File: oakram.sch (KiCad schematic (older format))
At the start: 4 parts, among them U1 DRAM_1MX16_SOJ, U2 DRAM_1MX16_SOJ, X1 ZIP40, X2 ZIP40

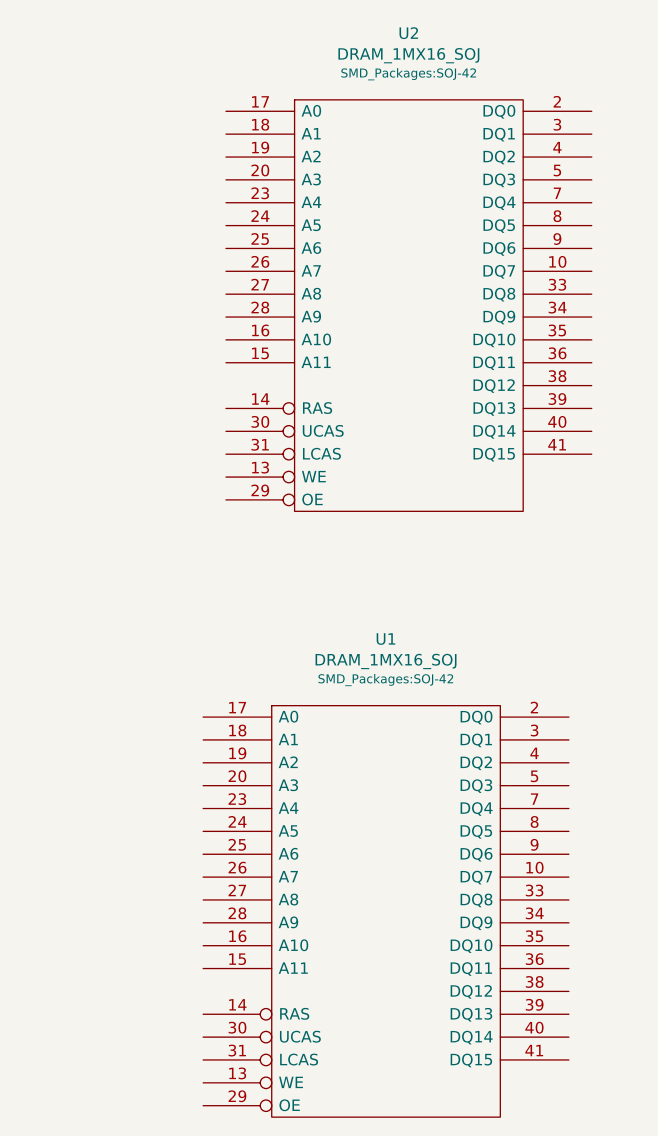
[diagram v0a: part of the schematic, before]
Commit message: Some bus signals assigned
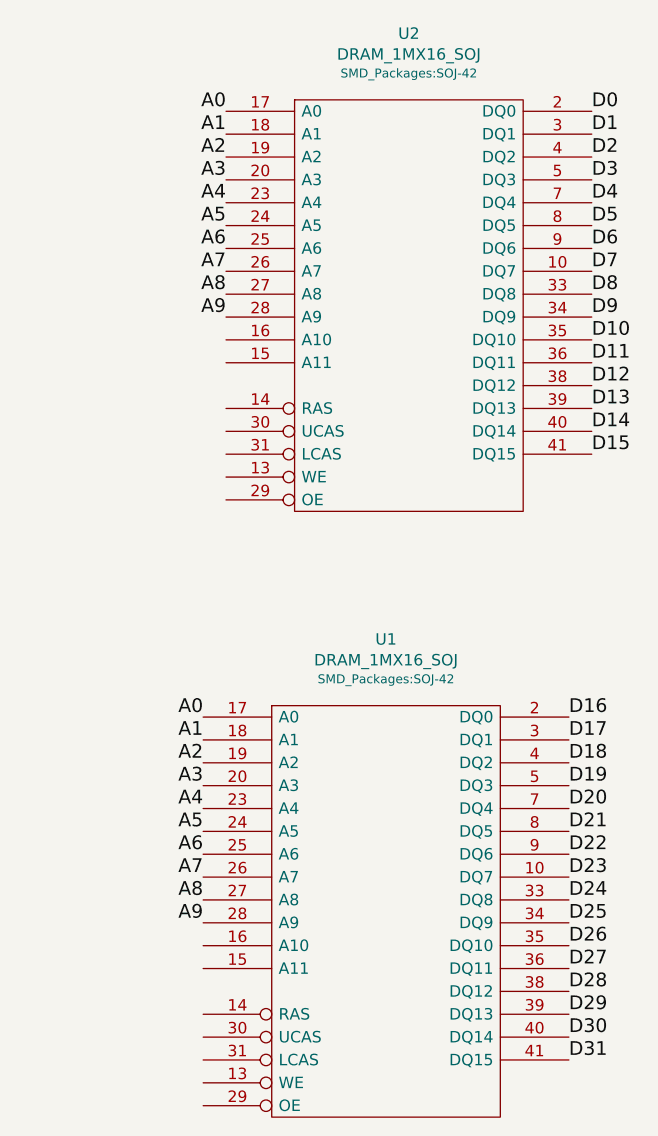
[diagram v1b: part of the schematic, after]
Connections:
- net A0: now also U1.17 (A0), U2.17 (A0)
- net A1: now also U1.18 (A1), U2.18 (A1)
- net A2: now also U1.19 (A2), U2.19 (A2)
- net A3: now also U1.20 (A3), U2.20 (A3)
- net A4: now also U1.23 (A4), U2.23 (A4)
- net A5: now also U1.24 (A5), U2.24 (A5)
- net A6: now also U1.25 (A6), U2.25 (A6)
- net A7: now also U1.26 (A7), U2.26 (A7)
- net A8: now also U1.27 (A8), U2.27 (A8)
- net A9: now also U1.28 (A9), U2.28 (A9)
- net D0: now also U2.2 (DQ0)
- net D1: now also U2.3 (DQ1)
- net D10: now also U2.35 (DQ10)
- net D11: now also U2.36 (DQ11)
- net D12: now also U2.38 (DQ12)
- net D13: now also U2.39 (DQ13)
- net D14: now also U2.40 (DQ14)
- net D15: now also U2.41 (DQ15)
- net D16: now also U1.2 (DQ0)
- net D17: now also U1.3 (DQ1)
- net D18: now also U1.4 (DQ2)
- net D19: now also U1.5 (DQ3)
- net D2: now also U2.4 (DQ2)
- net D20: now also U1.7 (DQ4)
- net D21: now also U1.8 (DQ5)
- net D22: now also U1.9 (DQ6)
- net D23: now also U1.10 (DQ7)
- net D24: now also U1.33 (DQ8)
- net D25: now also U1.34 (DQ9)
- net D26: now also U1.35 (DQ10)
- net D27: now also U1.36 (DQ11)
- net D28: now also U1.38 (DQ12)
- net D29: now also U1.39 (DQ13)
- net D3: now also U2.5 (DQ3)
- net D30: now also U1.40 (DQ14)
- net D31: now also U1.41 (DQ15)
- net D4: now also U2.7 (DQ4)
- net D5: now also U2.8 (DQ5)
- net D6: now also U2.9 (DQ6)
- net D7: now also U2.10 (DQ7)
- net D8: now also U2.33 (DQ8)
- net D9: now also U2.34 (DQ9)
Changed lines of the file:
@@
 LIBS:valves
 LIBS:oakram
+LIBS:oakram-cache
 EELAYER 26 0
 EELAYER END
@@
 	1    0    0    -1
 $EndComp
+Text Label 7750 875  2    60   ~ 0
+A0
+Text Label 7750 975  2    60   ~ 0
+A1
+Text Label 7750 1075 2    60   ~ 0
+A2
+Text Label 7750 1175 2    60   ~ 0
+A3
+Text Label 7750 1275 2    60   ~ 0
+A4
+Text Label 7750 1375 2    60   ~ 0
+A5
+Text Label 7750 1475 2    60   ~ 0
+A6
+Text Label 7750 1575 2    60   ~ 0
+A7
+Text Label 7750 1675 2    60   ~ 0
+A8
+Text Label 7750 1775 2    60   ~ 0
+A9
+Text Label 7650 3525 2    60   ~ 0
+A0
+Text Label 7650 3625 2    60   ~ 0
+A1
+Text Label 7650 3725 2    60   ~ 0
+A2
+Text Label 7650 3825 2    60   ~ 0
+A3
+Text Label 7650 3925 2    60   ~ 0
+A4
+Text Label 7650 4025 2    60   ~ 0
+A5
+Text Label 7650 4125 2    60   ~ 0
+A6
+Text Label 7650 4225 2    60   ~ 0
+A7
+Text Label 7650 4325 2    60   ~ 0
+A8
+Text Label 7650 4425 2    60   ~ 0
+A9
+Text Label 9250 3525 0    60   ~ 0
+D16
+Text Label 9250 3625 0    60   ~ 0
+D17
+Text Label 9250 3725 0    60   ~ 0
+D18
+Text Label 9250 3825 0    60   ~ 0
+D19
+Text Label 9250 3925 0    60   ~ 0
+D20
+Text Label 9250 4025 0    60   ~ 0
+D21
+Text Label 9250 4125 0    60   ~ 0
+D22
+Text Label 9250 4225 0    60   ~ 0
+D23
+Text Label 9250 4325 0    60   ~ 0
+D24
+Text Label 9250 4425 0    60   ~ 0
+D25
+Text Label 9250 4525 0    60   ~ 0
+D26
+Text Label 9250 4625 0    60   ~ 0
+D27
+Text Label 9250 4725 0    60   ~ 0
+D28
+Text Label 9250 4825 0    60   ~ 0
+D29
+Text Label 9250 4925 0    60   ~ 0
+D30
+Text Label 9250 5025 0    60   ~ 0
+D31
+Text Label 9350 875  0    60   ~ 0
+D0
+Text Label 9350 975  0    60   ~ 0
+D1
+Text Label 9350 1075 0    60   ~ 0
+D2
+Text Label 9350 1175 0    60   ~ 0
+D3
+Text Label 9350 1275 0    60   ~ 0
+D4
+Text Label 9350 1375 0    60   ~ 0
+D5
+Text Label 9350 1475 0    60   ~ 0
+D6
+Text Label 9350 1575 0    60   ~ 0
+D7
+Text Label 9350 1675 0    60   ~ 0
+D8
+Text Label 9350 1775 0    60   ~ 0
+D9
+Text Label 9350 1875 0    60   ~ 0
+D10
+Text Label 9350 1975 0    60   ~ 0
+D11
+Text Label 9350 2075 0    60   ~ 0
+D12
+Text Label 9350 2175 0    60   ~ 0
+D13
+Text Label 9350 2275 0    60   ~ 0
+D14
+Text Label 9350 2375 0    60   ~ 0
+D15
 $EndSCHEMATC

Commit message: Moar
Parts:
- U1, U2: value DRAM_1MX16_SOJ -> IS41C16105C
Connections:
- net +5VDC is gone; now on net VCC: X1.11 (Vcc), X1.16 (Vcc), X1.30 (Vcc), X2.11 (Vcc), X2.16 (Vcc), X2.30 (Vcc)
- net D10: now also U2.39 (DQ13); no longer U2.35 (DQ10)
- net D11: now also U2.38 (DQ12); no longer U2.36 (DQ11)
- net D12: now also U2.36 (DQ11); no longer U2.38 (DQ12)
- net D13: now also U2.35 (DQ10); no longer U2.39 (DQ13)
- net D14: now also U2.34 (DQ9); no longer U2.40 (DQ14)
- net D15: now also U2.33 (DQ8); no longer U2.41 (DQ15)
- net D16: now also U1.41 (DQ15); no longer U1.2 (DQ0)
- net D17: now also U1.40 (DQ14); no longer U1.3 (DQ1)
- net D18: now also U1.39 (DQ13); no longer U1.4 (DQ2)
- net D19: now also U1.38 (DQ12); no longer U1.5 (DQ3)
- net D20: now also U1.36 (DQ11); no longer U1.7 (DQ4)
- net D21: now also U1.35 (DQ10); no longer U1.8 (DQ5)
- net D22: now also U1.34 (DQ9); no longer U1.9 (DQ6)
- net D23: now also U1.33 (DQ8); no longer U1.10 (DQ7)
- net D24: now also U1.2 (DQ0); no longer U1.33 (DQ8)
- net D25: now also U1.3 (DQ1); no longer U1.34 (DQ9)
- net D26: now also U1.4 (DQ2); no longer U1.35 (DQ10)
- net D27: now also U1.5 (DQ3); no longer U1.36 (DQ11)
- net D28: now also U1.7 (DQ4); no longer U1.38 (DQ12)
- net D29: now also U1.8 (DQ5); no longer U1.39 (DQ13)
- net D30: now also U1.9 (DQ6); no longer U1.40 (DQ14)
- net D31: now also U1.10 (DQ7); no longer U1.41 (DQ15)
- net D8: now also U2.41 (DQ15); no longer U2.33 (DQ8)
- net D9: now also U2.40 (DQ14); no longer U2.34 (DQ9)
- net ~CAS0: now also U2.31 (LCAS)
- net ~CAS1: now also U2.30 (UCAS)
- net ~CAS2: now also U1.31 (LCAS)
- net ~CAS3: now also U1.30 (UCAS)
- net ~OE: now also U1.29 (OE), U2.29 (OE)
- net ~RAS: now also U1.14 (RAS), U2.14 (RAS)
- net ~WE: now also U1.13 (WE), U2.13 (WE)
- no-connect marks 6 -> 10
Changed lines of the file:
@@
 $EndComp
 Text GLabel 3500 1350 0    60   Output ~ 0
-+5VDC
+VCC
 Text GLabel 5350 1550 2    60   Output ~ 0
-+5VDC
+VCC
 NoConn ~ 3950 1850
 NoConn ~ 4750 2750
@@
 	3950 2550 3600 2550
 Text GLabel 5400 2250 2    60   Output ~ 0
-+5VDC
+VCC
 $Comp
 L GND #PWR03
@@
 $EndComp
 Text GLabel 3500 3675 0    60   Output ~ 0
-+5VDC
+VCC
 Text GLabel 5350 3875 2    60   Output ~ 0
-+5VDC
+VCC
 NoConn ~ 3950 4175
 NoConn ~ 4750 5075
@@
 	3950 4875 3600 4875
 Text GLabel 5400 4575 2    60   Output ~ 0
-+5VDC
+VCC
 $Comp
 L GND #PWR06
@@
 P 8550 1725
 F 0 "U2" H 8550 2915 50  0000 C CNN
-F 1 "DRAM_1MX16_SOJ" H 8550 2824 50  0000 C CNN
+F 1 "IS41C16105C" H 8550 2824 50  0000 C CNN
 F 2 "SMD_Packages:SOJ-42" H 8550 2741 39  0000 C CNN
 F 3 "" H 8550 1725 50  0001 C CNN
@@
 P 8450 4375
 F 0 "U1" H 8450 5565 50  0000 C CNN
-F 1 "DRAM_1MX16_SOJ" H 8450 5474 50  0000 C CNN
+F 1 "IS41C16105C" H 8450 5474 50  0000 C CNN
 F 2 "SMD_Packages:SOJ-42" H 8450 5391 39  0000 C CNN
 F 3 "" H 8450 4375 50  0001 C CNN
@@
 Text Label 7650 4425 2    60   ~ 0
 A9
-Text Label 9250 3525 0    60   ~ 0
+Text Label 9250 5025 0    60   ~ 0
 D16
-Text Label 9250 3625 0    60   ~ 0
+Text Label 9250 4925 0    60   ~ 0
 D17
-Text Label 9250 3725 0    60   ~ 0
+Text Label 9250 4825 0    60   ~ 0
 D18
-Text Label 9250 3825 0    60   ~ 0
+Text Label 9250 4725 0    60   ~ 0
 D19
-Text Label 9250 3925 0    60   ~ 0
+Text Label 9250 4625 0    60   ~ 0
 D20
-Text Label 9250 4025 0    60   ~ 0
+Text Label 9250 4525 0    60   ~ 0
 D21
-Text Label 9250 4125 0    60   ~ 0
+Text Label 9250 4425 0    60   ~ 0
 D22
-Text Label 9250 4225 0    60   ~ 0
-D23
 Text Label 9250 4325 0    60   ~ 0
+D23
+Text Label 9250 3525 0    60   ~ 0
 D24
-Text Label 9250 4425 0    60   ~ 0
+Text Label 9250 3625 0    60   ~ 0
 D25
-Text Label 9250 4525 0    60   ~ 0
+Text Label 9250 3725 0    60   ~ 0
 D26
-Text Label 9250 4625 0    60   ~ 0
+Text Label 9250 3825 0    60   ~ 0
 D27
-Text Label 9250 4725 0    60   ~ 0
+Text Label 9250 3925 0    60   ~ 0
 D28
-Text Label 9250 4825 0    60   ~ 0
+Text Label 9250 4025 0    60   ~ 0
 D29
-Text Label 9250 4925 0    60   ~ 0
+Text Label 9250 4125 0    60   ~ 0
 D30
-Text Label 9250 5025 0    60   ~ 0
+Text Label 9250 4225 0    60   ~ 0
 D31
 Text Label 9350 875  0    60   ~ 0
@@
 Text Label 9350 1575 0    60   ~ 0
 D7
-Text Label 9350 1675 0    60   ~ 0
+Text Label 9350 2375 0    60   ~ 0
 D8
-Text Label 9350 1775 0    60   ~ 0
+Text Label 9350 2275 0    60   ~ 0
 D9
-Text Label 9350 1875 0    60   ~ 0
+Text Label 9350 2175 0    60   ~ 0
 D10
-Text Label 9350 1975 0    60   ~ 0
-D11
 Text Label 9350 2075 0    60   ~ 0
+D11
+Text Label 9350 1975 0    60   ~ 0
 D12
-Text Label 9350 2175 0    60   ~ 0
+Text Label 9350 1875 0    60   ~ 0
 D13
-Text Label 9350 2275 0    60   ~ 0
+Text Label 9350 1775 0    60   ~ 0
 D14
-Text Label 9350 2375 0    60   ~ 0
+Text Label 9350 1675 0    60   ~ 0
 D15
+Text Label 7750 2475 2    60   ~ 0
+~WE
+Text Label 7650 5125 2    60   ~ 0
+~WE
+Text Label 7650 5225 2    60   ~ 0
+~OE
+Text Label 7750 2575 2    60   ~ 0
+~OE
+Text Label 7750 2175 2    60   ~ 0
+~RAS
+Text Label 7650 4825 2    60   ~ 0
+~RAS
+Text Label 7750 2375 2    60   ~ 0
+~CAS0
+Text Label 7750 2275 2    60   ~ 0
+~CAS1
+Text Label 7650 5025 2    60   ~ 0
+~CAS2
+Text Label 7650 4925 2    60   ~ 0
+~CAS3
+NoConn ~ 7750 1875
+NoConn ~ 7750 1975
+NoConn ~ 7650 4525
+NoConn ~ 7650 4625
 $EndSCHEMATC

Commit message: Up
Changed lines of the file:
@@
 Text Label 4950 2150 0    60   ~ 0
 A2
-Text Label 4950 2350 0    60   ~ 0
+Text Label 5100 2350 0    60   ~ 0
 A4
-Text Label 4950 2450 0    60   ~ 0
+Text Label 5100 2450 0    60   ~ 0
 A6
-Text Label 4950 2550 0    60   ~ 0
+Text Label 5100 2550 0    60   ~ 0
 A8
 Text Label 3600 2150 2    60   ~ 0
@@
 Text Label 3600 2250 2    60   ~ 0
 A3
-Text Label 3600 2450 2    60   ~ 0
+Text Label 3450 2450 2    60   ~ 0
 A5
-Text Label 3600 2550 2    60   ~ 0
+Text Label 3450 2550 2    60   ~ 0
 A7
 Wire Wire Line
@@
 NoConn ~ 4750 5075
 NoConn ~ 3950 4375
-Text Label 4950 4375 0    60   ~ 0
+Text Label 5100 4400 0    60   ~ 0
 A0
-Text Label 4950 4475 0    60   ~ 0
+Text Label 5050 4500 0    60   ~ 0
 A2
 Text Label 4950 4675 0    60   ~ 0
@@
 Text Label 4950 4875 0    60   ~ 0
 A8
-Text Label 3600 4475 2    60   ~ 0
+Text Label 3350 4500 2    60   ~ 0
 A1
-Text Label 3600 4575 2    60   ~ 0
+Text Label 3350 4600 2    60   ~ 0
 A3
 Text Label 3600 4775 2    60   ~ 0
@@
 Wire Wire Line
 	4750 4175 4950 4175
-Text Label 4950 4175 0    60   ~ 0
+Text Label 5050 4150 0    60   ~ 0
 A9
 Text Label 3600 3175 2    60   ~ 0
@@
 Wire Wire Line
 	3950 4275 3600 4275
-Text Label 3600 4275 2    60   ~ 0
+Text Label 3450 4300 2    60   ~ 0
 ~WE
 Wire Wire Line
 	4750 4275 5100 4275
-Text Label 5100 4275 0    60   ~ 0
+Text Label 5200 4300 0    60   ~ 0
 ~RAS
 Wire Wire Line

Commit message: Added caps
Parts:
- added C1, C2, C3, C4, C5, C6: 2,2u, Capacitors_SMD:C_0805, symbol C
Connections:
- net labels added: VSS
- net labels removed: GND
- wire segments 68 -> 82
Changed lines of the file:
@@
 	1    0    0    -1
 $EndComp
-$Comp
-L GND #PWR01
-U 1 1 59C97BC1
-P 3950 1050
-F 0 "#PWR01" H 3950 800 50  0001 C CNN
-F 1 "GND" V 3955 922 50  0000 R CNN
-F 2 "" H 3950 1050 50  0001 C CNN
-F 3 "" H 3950 1050 50  0001 C CNN
-	1    3950 1050
-	0    1    1    0
-$EndComp
-$Comp
-L GND #PWR02
-U 1 1 59C97BD9
-P 4750 1250
-F 0 "#PWR02" H 4750 1000 50  0001 C CNN
-F 1 "GND" V 4755 1122 50  0000 R CNN
-F 2 "" H 4750 1250 50  0001 C CNN
-F 3 "" H 4750 1250 50  0001 C CNN
-	1    4750 1250
-	0    -1   -1   0
-$EndComp
 Text GLabel 3500 1350 0    60   Output ~ 0
 VCC
@@
 Text GLabel 5400 2250 2    60   Output ~ 0
 VCC
-$Comp
-L GND #PWR03
-U 1 1 59C97DF8
-P 3950 2350
-F 0 "#PWR03" H 3950 2100 50  0001 C CNN
-F 1 "GND" V 3955 2222 50  0000 R CNN
-F 2 "" H 3950 2350 50  0001 C CNN
-F 3 "" H 3950 2350 50  0001 C CNN
-	1    3950 2350
-	0    1    1    0
-$EndComp
 Wire Wire Line
 	4750 2250 5400 2250
@@
 	1    0    0    -1
 $EndComp
-$Comp
-L GND #PWR04
-U 1 1 59C98340
-P 3950 3375
-F 0 "#PWR04" H 3950 3125 50  0001 C CNN
-F 1 "GND" V 3955 3247 50  0000 R CNN
-F 2 "" H 3950 3375 50  0001 C CNN
-F 3 "" H 3950 3375 50  0001 C CNN
-	1    3950 3375
-	0    1    1    0
-$EndComp
-$Comp
-L GND #PWR05
-U 1 1 59C98346
-P 4750 3575
-F 0 "#PWR05" H 4750 3325 50  0001 C CNN
-F 1 "GND" V 4755 3447 50  0000 R CNN
-F 2 "" H 4750 3575 50  0001 C CNN
-F 3 "" H 4750 3575 50  0001 C CNN
-	1    4750 3575
-	0    -1   -1   0
-$EndComp
 Text GLabel 3500 3675 0    60   Output ~ 0
 VCC
@@
 Text GLabel 5400 4575 2    60   Output ~ 0
 VCC
-$Comp
-L GND #PWR06
-U 1 1 59C98364
-P 3950 4675
-F 0 "#PWR06" H 3950 4425 50  0001 C CNN
-F 1 "GND" V 3955 4547 50  0000 R CNN
-F 2 "" H 3950 4675 50  0001 C CNN
-F 3 "" H 3950 4675 50  0001 C CNN
-	1    3950 4675
-	0    1    1    0
-$EndComp
 Wire Wire Line
 	4750 4575 5400 4575
@@
 Text Label 7750 2275 2    60   ~ 0
 ~CAS1
-Text Label 7650 5025 2    60   ~ 0
-~CAS2
 Text Label 7650 4925 2    60   ~ 0
+~CAS2
+Text Label 7650 5025 2    60   ~ 0
 ~CAS3
 NoConn ~ 7750 1875
@@
 NoConn ~ 7650 4525
 NoConn ~ 7650 4625
+Text GLabel 3950 1050 0    60   UnSpc ~ 0
+VSS
+Text GLabel 4750 1250 2    60   UnSpc ~ 0
+VSS
+Text GLabel 3950 2350 0    60   UnSpc ~ 0
+VSS
+Text GLabel 3950 4675 0    60   UnSpc ~ 0
+VSS
+Text GLabel 3950 3375 0    60   UnSpc ~ 0
+VSS
+Text GLabel 4750 3575 2    60   UnSpc ~ 0
+VSS
+Text GLabel 2525 5975 0    60   Output ~ 0
+VCC
+Wire Wire Line
+	2525 5975 5275 5975
+$Comp
+L C C1
+U 1 1 59CBE190
+P 2850 6250
+F 0 "C1" H 2965 6333 50  0000 L CNN
+F 1 "2,2u" H 2965 6242 50  0000 L CNN
+F 2 "Capacitors_SMD:C_0805" H 2965 6159 39  0000 L CNN
+F 3 "" H 2850 6250 50  0001 C CNN
+	1    2850 6250
+	1    0    0    -1
+$EndComp
+Text GLabel 2525 6575 0    60   UnSpc ~ 0
+VSS
+Wire Wire Line
+	2850 6100 2850 5975
+Connection ~ 2850 5975
+Wire Wire Line
+	2525 6575 5275 6575
+Wire Wire Line
+	2850 6400 2850 6575
+Connection ~ 2850 6575
+$Comp
+L C C2
+U 1 1 59CBE35E
+P 3350 6250
+F 0 "C2" H 3465 6333 50  0000 L CNN
+F 1 "2,2u" H 3465 6242 50  0000 L CNN
+F 2 "Capacitors_SMD:C_0805" H 3465 6159 39  0000 L CNN
+F 3 "" H 3350 6250 50  0001 C CNN
+	1    3350 6250
+	1    0    0    -1
+$EndComp
+$Comp
+L C C3
+U 1 1 59CBE39E
+P 3800 6250
+F 0 "C3" H 3915 6333 50  0000 L CNN
+F 1 "2,2u" H 3915 6242 50  0000 L CNN
+F 2 "Capacitors_SMD:C_0805" H 3915 6159 39  0000 L CNN
+F 3 "" H 3800 6250 50  0001 C CNN
+	1    3800 6250
+	1    0    0    -1
+$EndComp
+$Comp
+L C C4
+U 1 1 59CBE4F8
+P 4325 6250
+F 0 "C4" H 4440 6333 50  0000 L CNN
+F 1 "2,2u" H 4440 6242 50  0000 L CNN
+F 2 "Capacitors_SMD:C_0805" H 4440 6159 39  0000 L CNN
+F 3 "" H 4325 6250 50  0001 C CNN
+	1    4325 6250
+	1    0    0    -1
+$EndComp
+Wire Wire Line
+	4325 6100 4325 5975
+Wire Wire Line
+	4325 6400 4325 6575
+$Comp
+L C C5
+U 1 1 59CBE500
+P 4825 6250
+F 0 "C5" H 4940 6333 50  0000 L CNN
+F 1 "2,2u" H 4940 6242 50  0000 L CNN
+F 2 "Capacitors_SMD:C_0805" H 4940 6159 39  0000 L CNN
+F 3 "" H 4825 6250 50  0001 C CNN
+	1    4825 6250
+	1    0    0    -1
+$EndComp
+$Comp
+L C C6
+U 1 1 59CBE506
+P 5275 6250
+F 0 "C6" H 5390 6333 50  0000 L CNN
+F 1 "2,2u" H 5390 6242 50  0000 L CNN
+F 2 "Capacitors_SMD:C_0805" H 5390 6159 39  0000 L CNN
+F 3 "" H 5275 6250 50  0001 C CNN
+	1    5275 6250
+	1    0    0    -1
+$EndComp
+Wire Wire Line
+	5275 5975 5275 6100
+Wire Wire Line
+	3350 6100 3350 5975
+Connection ~ 3350 5975
+Wire Wire Line
+	5275 6575 5275 6400
+Wire Wire Line
+	3350 6400 3350 6575
+Connection ~ 3350 6575
+Wire Wire Line
+	3800 6100 3800 5975
+Connection ~ 3800 5975
+Wire Wire Line
+	4825 6100 4825 5975
+Connection ~ 4825 5975
+Wire Wire Line
+	4825 6400 4825 6575
+Connection ~ 4825 6575
+Wire Wire Line
+	3800 6400 3800 6575
+Connection ~ 3800 6575
+Connection ~ 4325 6575
+Connection ~ 4325 5975
 $EndSCHEMATC

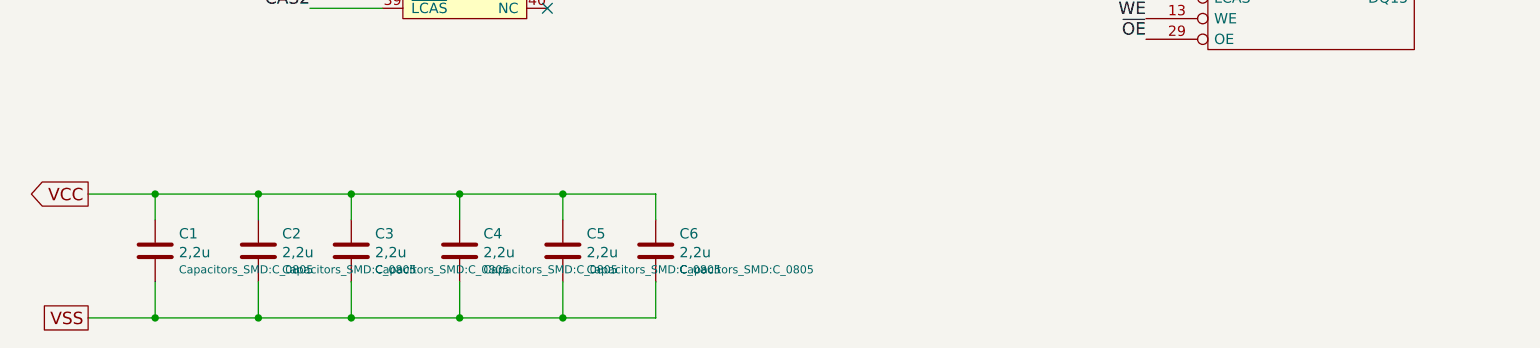
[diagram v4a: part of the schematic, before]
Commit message: Added elcap
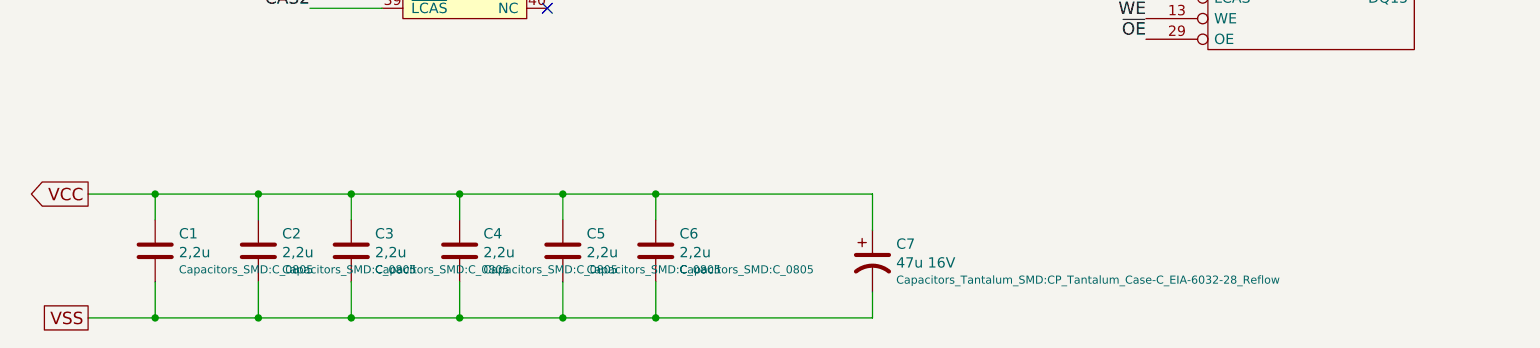
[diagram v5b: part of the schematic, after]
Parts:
- added C7: 47u 16V, Capacitors_Tantalum_SMD:CP_Tantalum_Case-C_EIA-6032-28_Reflow, symbol CP1
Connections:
- wire segments 82 -> 84
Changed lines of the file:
@@
 VCC
 Wire Wire Line
-	2525 5975 5275 5975
+	2525 5975 6325 5975
 $Comp
 L C C1
@@
 Connection ~ 2850 5975
 Wire Wire Line
-	2525 6575 5275 6575
+	2525 6575 6325 6575
 Wire Wire Line
 	2850 6400 2850 6575
@@
 Connection ~ 4325 6575
 Connection ~ 4325 5975
+$Comp
+L CP1 C7
+U 1 1 59CA5A3F
+P 6325 6300
+F 0 "C7" H 6440 6383 50  0000 L CNN
+F 1 "47u 16V" H 6440 6292 50  0000 L CNN
+F 2 "Capacitors_Tantalum_SMD:CP_Tantalum_Case-C_EIA-6032-28_Reflow" H 6440 6209 39  0000 L CNN
+F 3 "" H 6325 6300 50  0001 C CNN
+	1    6325 6300
+	1    0    0    -1
+$EndComp
+Wire Wire Line
+	6325 6575 6325 6450
+Connection ~ 5275 6575
+Wire Wire Line
+	6325 5975 6325 6150
+Connection ~ 5275 5975
 $EndSCHEMATC
